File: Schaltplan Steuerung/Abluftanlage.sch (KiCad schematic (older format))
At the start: 27 parts, among them K1 6K4, K2 6K2, K3 6K1.1, K4 RELAY-CONTACTOR-3xCLOSE-3xCLO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, P1 CONN_01X03, P10 CONN_01X03, P11 CONN_01X02, P12 CONN_01X02, P13 CONN_01X01, P14 CONN_01X01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

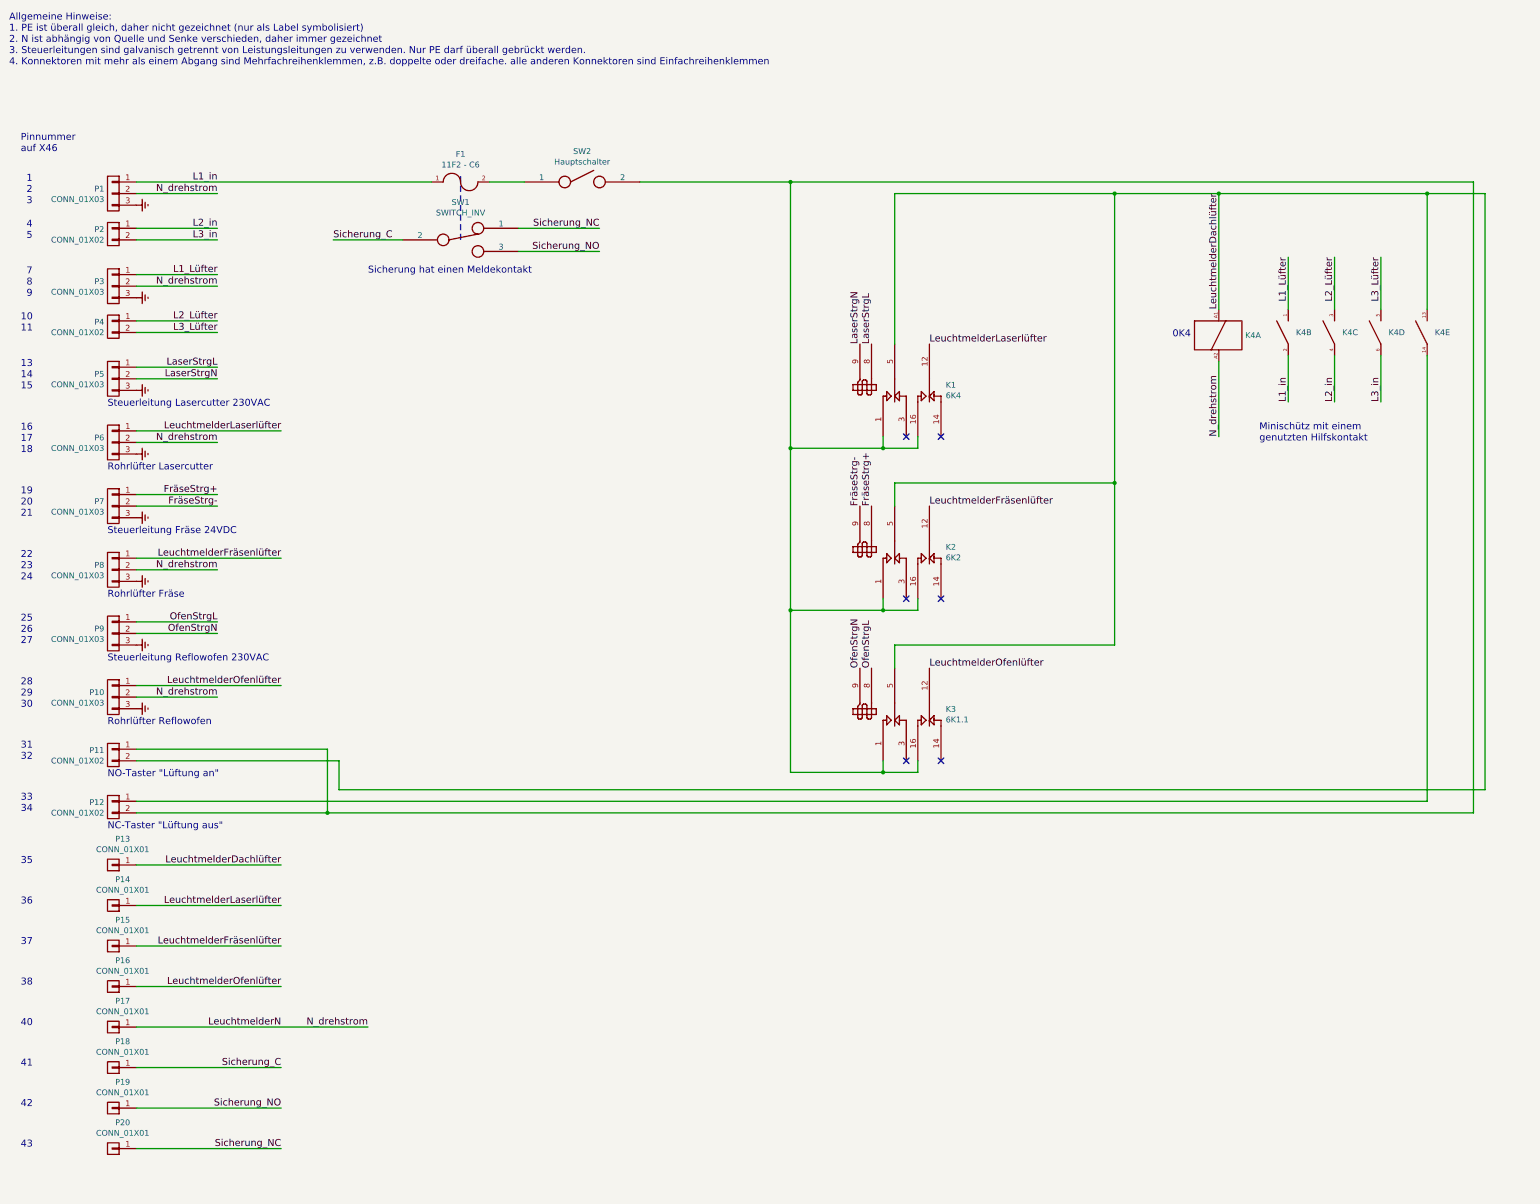
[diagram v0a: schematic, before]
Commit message: Kabelnummern für Lüfter-Fernsteuerung nachgetragen
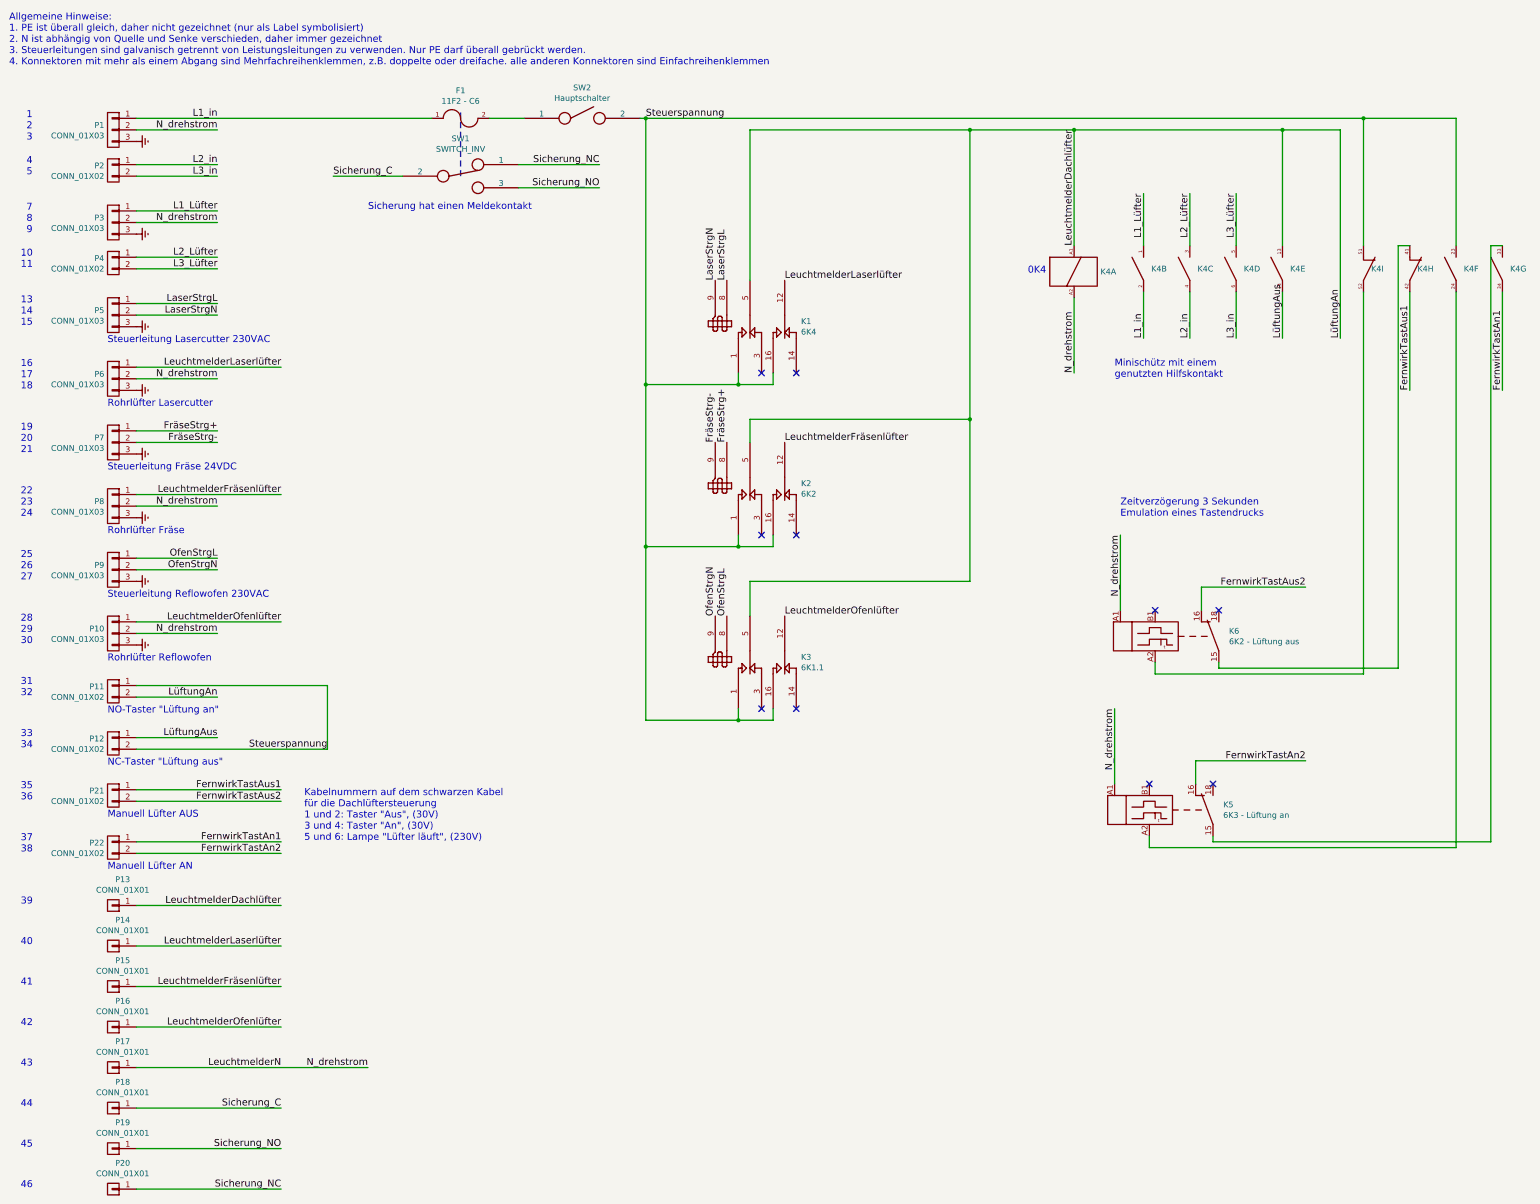
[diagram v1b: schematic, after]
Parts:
- added unit 6 of K4
- added unit 7 of K4
- added unit 8 of K4
- added unit 9 of K4
- added K5: 6K3 - Lüftung an, symbol RELAY-DELAY-1XCHANGE_FINDER_87.41
- added K6: 6K2 - Lüftung aus, symbol RELAY-DELAY-1XCHANGE_FINDER_87.41
- added P21, P22: CONN_01X02, symbol CONN_01X02
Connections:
- net LeuchtmelderN: now also K5.A1, K6.A1
- net Steuerspannung: now reaches K1.1 (T1), K1.16 (T2), K2.1 (T1), K2.16 (T2), K3.1 (T1), K3.16 (T2), P11.1 (P1), P12.2 (P2), SW2.2
- net Steuerspannung: now also K4.23, K4.51
- net LüftungAus: now reaches K4.14, P12.1 (P1)
- new net: K4.24, K5.A2
- new net: K4.33, K5.15
- new net: K4.41, K6.15
- new net: K4.52, K6.A2
- new net FernwirkTastAn1: K4.34, P22.1 (P1)
- new net FernwirkTastAn2: K5.16, P22.2 (P2)
- new net FernwirkTastAus1: K4.42, P21.1 (P1)
- new net FernwirkTastAus2: K6.16, P21.2 (P2)
- no-connect marks 6 -> 10
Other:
- note added: "35\n36"
- note added: "37\n38"
- note added: "39"
- note added: "44"
- note added: "45"
- note added: "46"
- note added: "Kabelnummern auf dem schwarzen Kabel\nfür die Dachlüftersteuerung\n1 und 2: Taster "Aus", (30V)\n3 und 4: Taster "An", (30V)\n5 und 6: Lampe "Lüfter läuft", (230V)"
- note added: "Manuell Lüfter AN"
- note added: "Manuell Lüfter AUS"
- note added: "Zeitverzögerung 3 Sekunden\nEmulation eines Tastendrucks"
- note removed: "35"
- note removed: "36"
- note removed: "37"
- note removed: "38"
- note removed: "Pinnummer\nauf X46"
- moved on the sheet: F1, K1, K2, K3, K4A, K4B, K4C, K4D, K4E, P1, P10, P11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

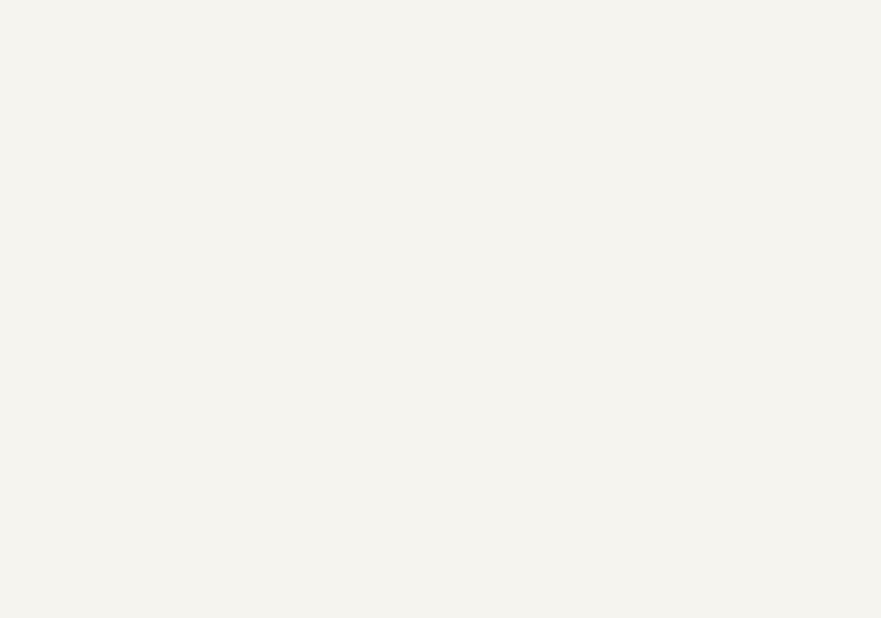
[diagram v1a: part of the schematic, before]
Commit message: Kabelnummern für Anzeigeelement hinzugefügt
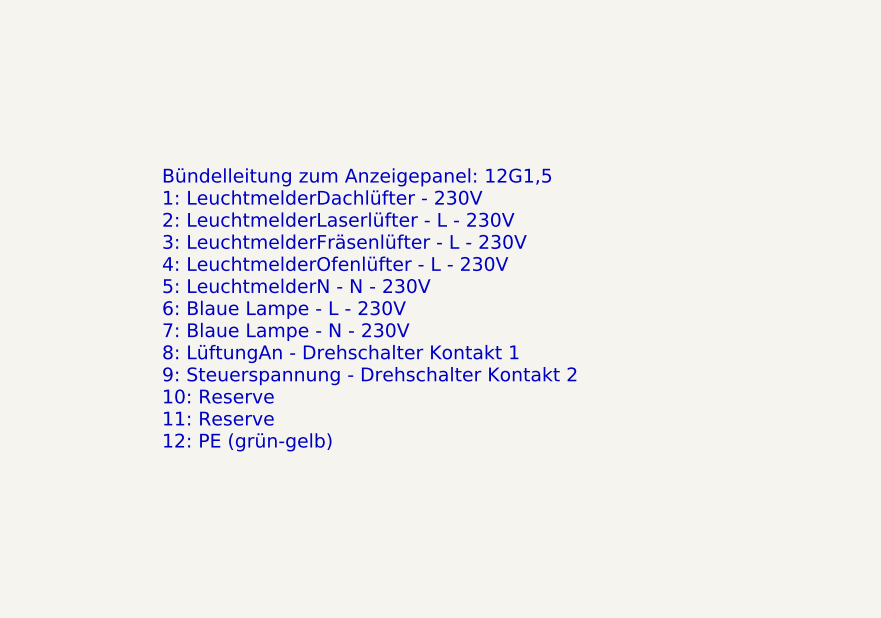
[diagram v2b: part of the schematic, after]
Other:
- note added: "Bündelleitung zum Anzeigepanel: 12G1,5\n1: LeuchtmelderDachlüfter - 230V\n2: LeuchtmelderLaserlüfter - L - 230V\n3: LeuchtmelderFräsenlüfter - L - 230V\n4: LeuchtmelderOfenlüfter - L - 230V\n5: LeuchtmelderN - N - 230V\n6: Blaue Lampe - L - 230V\n7: Blaue Lampe - N - 230V\n8: LüftungAn - Drehschalter Kontakt 1\n9: Steuerspannung - Drehschalter Kontakt 2\n10: Reserve\n11: Reserve\n12: PE (grün-gel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"
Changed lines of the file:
@@
 LIBS:switch-push
 LIBS:Abluftanlage-cache
-EELAYER 25 0
+EELAYER 26 0
 EELAYER END
 $Descr A3 16535 11693
@@
 Text Notes 3700 7900 0    60   ~ 0
 Kabelnummern auf dem schwarzen Kabel\nfür die Dachlüftersteuerung\n1 und 2: Taster "Aus", (30V)\n3 und 4: Taster "An", (30V)\n5 und 6: Lampe "Lüfter läuft", (230V)
+Text Notes 6250 9600 0    60   ~ 0
+Bündelleitung zum Anzeigepanel: 12G1,5\n1: LeuchtmelderDachlüfter - 230V\n2: LeuchtmelderLaserlüfter - L - 230V\n3: LeuchtmelderFräsenlüfter - L - 230V\n4: LeuchtmelderOfenlüfter - L - 230V\n5: LeuchtmelderN - N - 230V\n6: Blaue Lampe - L - 230V\n7: Blaue Lampe - N - 230V\n8: LüftungAn - Drehschalter Kontakt 1\n9: Steuerspannung - Drehschalter Kontakt 2\n10: Reserve\n11: Reserve\n12: PE (grün-gelb)
 $EndSCHEMATC
